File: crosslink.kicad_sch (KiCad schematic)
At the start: 2 parts, among them U9 CrossLink_LIF-MD6000-6JMG80I

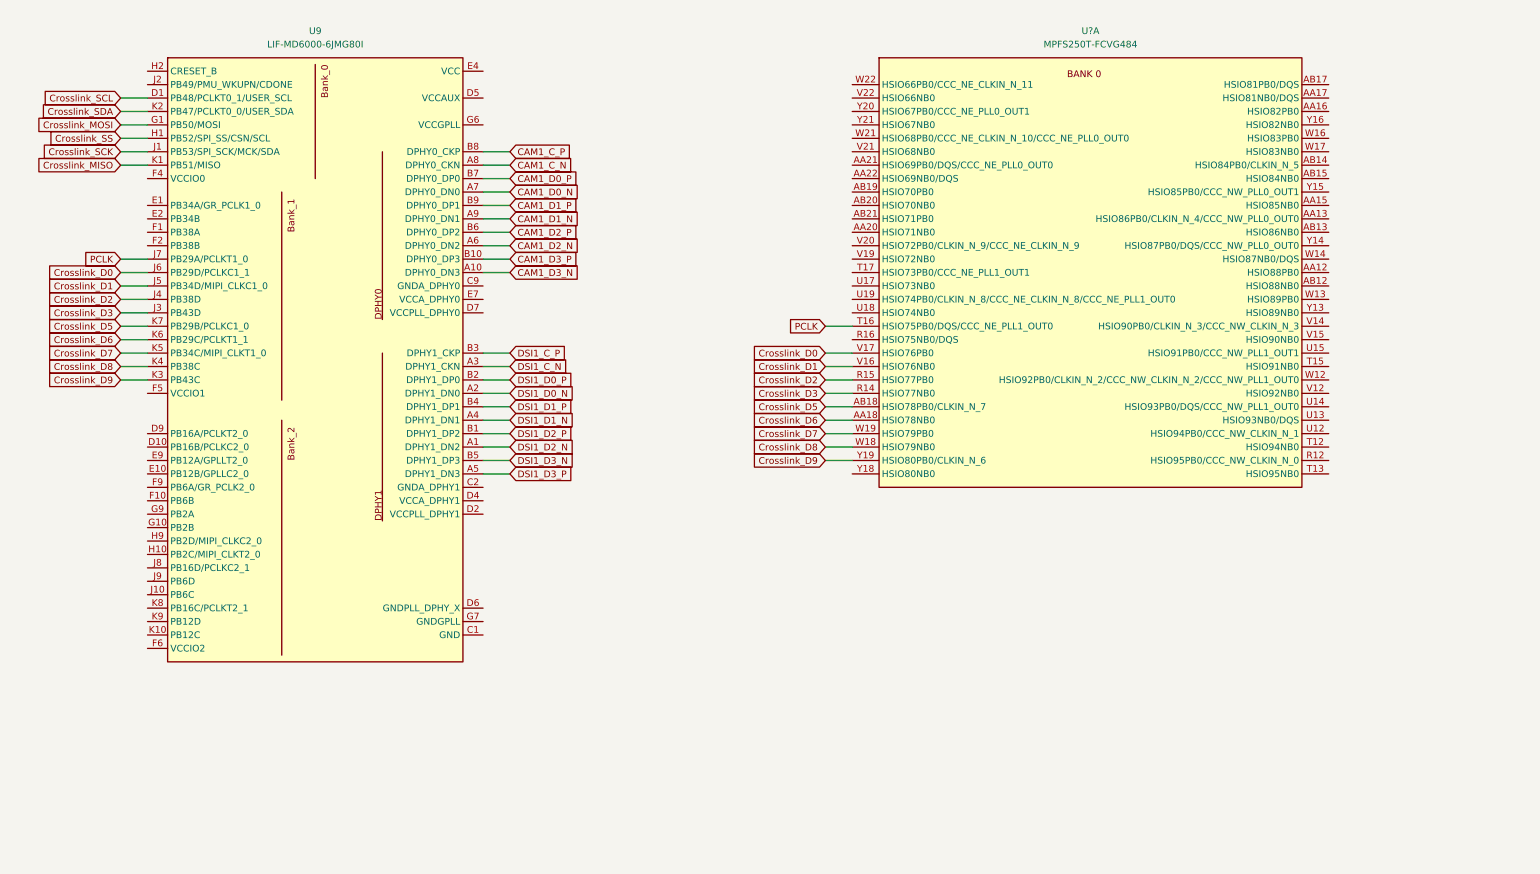
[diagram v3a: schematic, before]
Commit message: [#53847] Improve connection between Crosslink and PF
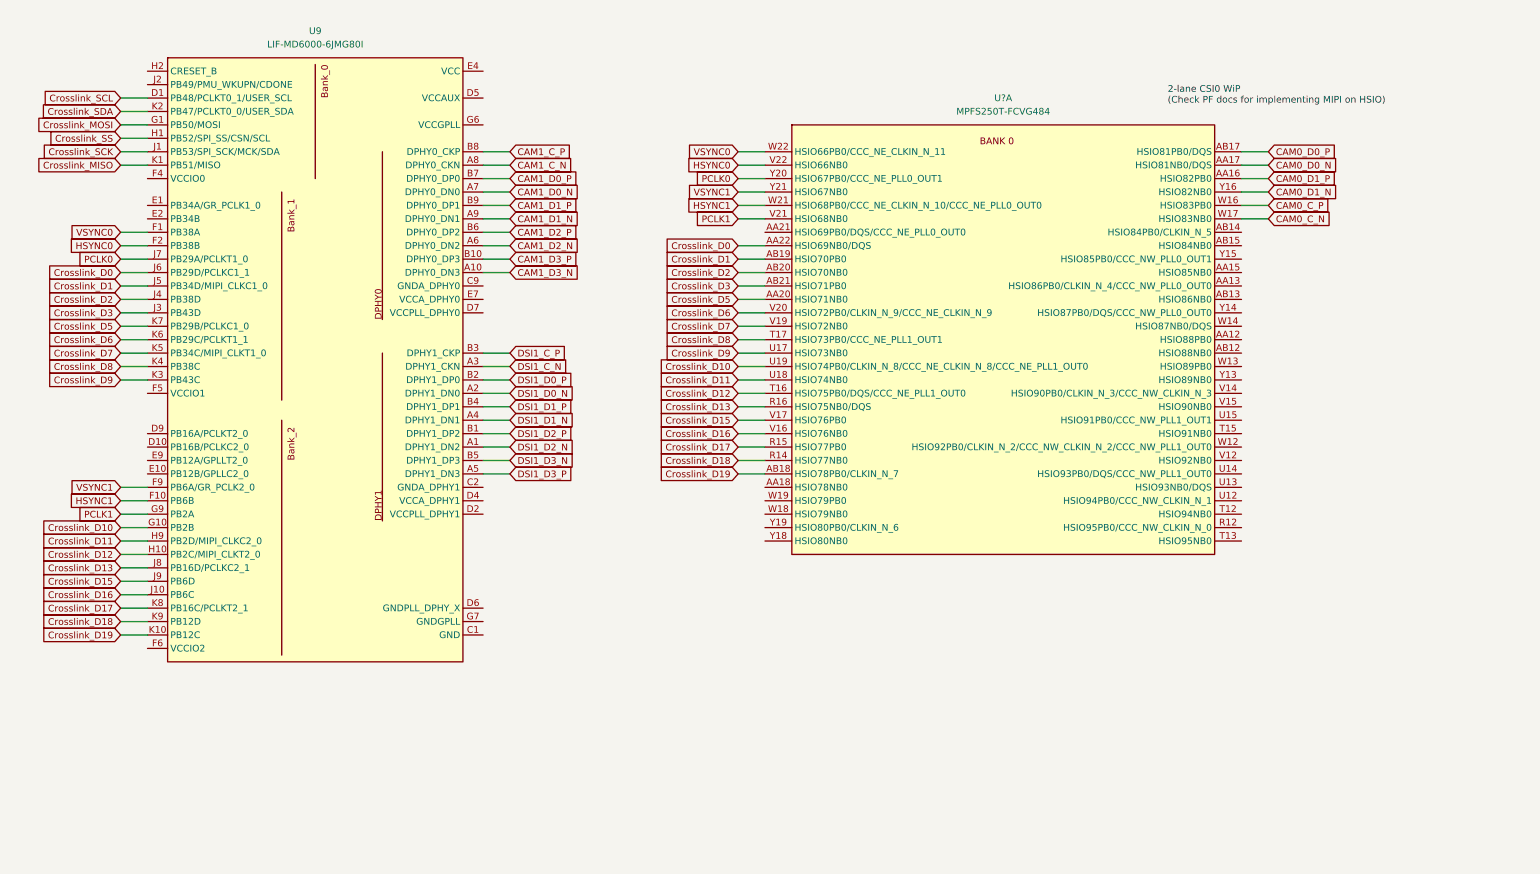
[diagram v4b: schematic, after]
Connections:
- net Crosslink_D0: now also U?.AA22 (HSIO69NB0/DQS); no longer U?.V17 (HSIO76PB0)
- net Crosslink_D1: now also U?.AB19 (HSIO70PB0); no longer U?.V16 (HSIO76NB0)
- net Crosslink_D2: now also U?.AB20 (HSIO70NB0); no longer U?.R15 (HSIO77PB0)
- net Crosslink_D3: now also U?.AB21 (HSIO71PB0); no longer U?.R14 (HSIO77NB0)
- net Crosslink_D5: now also U?.AA20 (HSIO71NB0); no longer U?.AB18 (HSIO78PB0/CLKIN_N_7)
- net Crosslink_D6: now also U?.V20 (HSIO72PB0/CLKIN_N_9/CCC_NE_CLKIN_N_9); no longer U?.AA18 (HSIO78NB0)
- net Crosslink_D7: now also U?.V19 (HSIO72NB0); no longer U?.W19 (HSIO79PB0)
- net Crosslink_D8: now also U?.T17 (HSIO73PB0/CCC_NE_PLL1_OUT1); no longer U?.W18 (HSIO79NB0)
- net Crosslink_D9: now also U?.U17 (HSIO73NB0); no longer U?.Y19 (HSIO80PB0/CLKIN_N_6)
- net CAM0_D1_P: now reaches U?.AA16 (HSIO82PB0)
- net CAM0_D0_N: now reaches U?.AA17 (HSIO81NB0/DQS)
- net CAM0_D0_P: now reaches U?.AB17 (HSIO81PB0/DQS)
- net Crosslink_D13: now reaches U?.R16 (HSIO75NB0/DQS)
- net Crosslink_D13: now also U9.J8 (PB16D/PCLKC2_1)
- net Crosslink_D11: now reaches U?.U18 (HSIO74NB0)
- net Crosslink_D11: now also U9.H9 (PB2D/MIPI_CLKC2_0)
- net Crosslink_D10: now reaches U?.U19 (HSIO74PB0/CLKIN_N_8/CCC_NE_CLKIN_N_8/CCC_NE_PLL1_OUT0)
- net Crosslink_D10: now also U9.G10 (PB2B)
- net PCLK1: now reaches U?.V21 (HSIO68NB0)
- net PCLK1: now also U9.G9 (PB2A)
- net HSYNC0: now reaches U?.V22 (HSIO66NB0)
- net HSYNC0: now also U9.F2 (PB38B)
- net CAM0_C_P: now reaches U?.W16 (HSIO83PB0)
- net CAM0_C_N: now reaches U?.W17 (HSIO83NB0)
- net HSYNC1: now reaches U?.W21 (HSIO68PB0/CCC_NE_CLKIN_N_10/CCC_NE_PLL0_OUT0)
- net HSYNC1: now also U9.F10 (PB6B)
- net VSYNC0: now reaches U?.W22 (HSIO66PB0/CCC_NE_CLKIN_N_11)
- net VSYNC0: now also U9.F1 (PB38A)
- net CAM0_D1_N: now reaches U?.Y16 (HSIO82NB0)
- net PCLK0: now reaches U?.Y20 (HSIO67PB0/CCC_NE_PLL0_OUT1)
- net PCLK0: now also U9.J7 (PB29A/PCLKT1_0)
- net VSYNC1: now reaches U?.Y21 (HSIO67NB0)
- net VSYNC1: now also U9.F9 (PB6A/GR_PCLK2_0)
- net Crosslink_D12: now reaches U9.H10 (PB2C/MIPI_CLKT2_0)
- net Crosslink_D12: now also U?.T16 (HSIO75PB0/DQS/CCC_NE_PLL1_OUT0)
- net Crosslink_D16: now reaches U9.J10 (PB6C)
- net Crosslink_D16: now also U?.V16 (HSIO76NB0)
- net Crosslink_D15: now reaches U9.J9 (PB6D)
- net Crosslink_D15: now also U?.V17 (HSIO76PB0)
- net Crosslink_D19: now reaches U9.K10 (PB12C)
- net Crosslink_D19: now also U?.AB18 (HSIO78PB0/CLKIN_N_7)
- net Crosslink_D17: now reaches U9.K8 (PB16C/PCLKT2_1)
- net Crosslink_D17: now also U?.R15 (HSIO77PB0)
- net Crosslink_D18: now reaches U9.K9 (PB12D)
- net Crosslink_D18: now also U?.R14 (HSIO77NB0)
- removed net PCLK: U9.J7 (PB29A/PCLKT1_0), U?.T16 (HSIO75PB0/DQS/CCC_NE_PLL1_OUT0)
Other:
- note added: "2-lane CSI0 WiP (Check PF docs for implementing MIPI on HSIO)"
- moved on the sheet: U?A

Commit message: [#53847] Add MIPI25 implementation of PF SoC
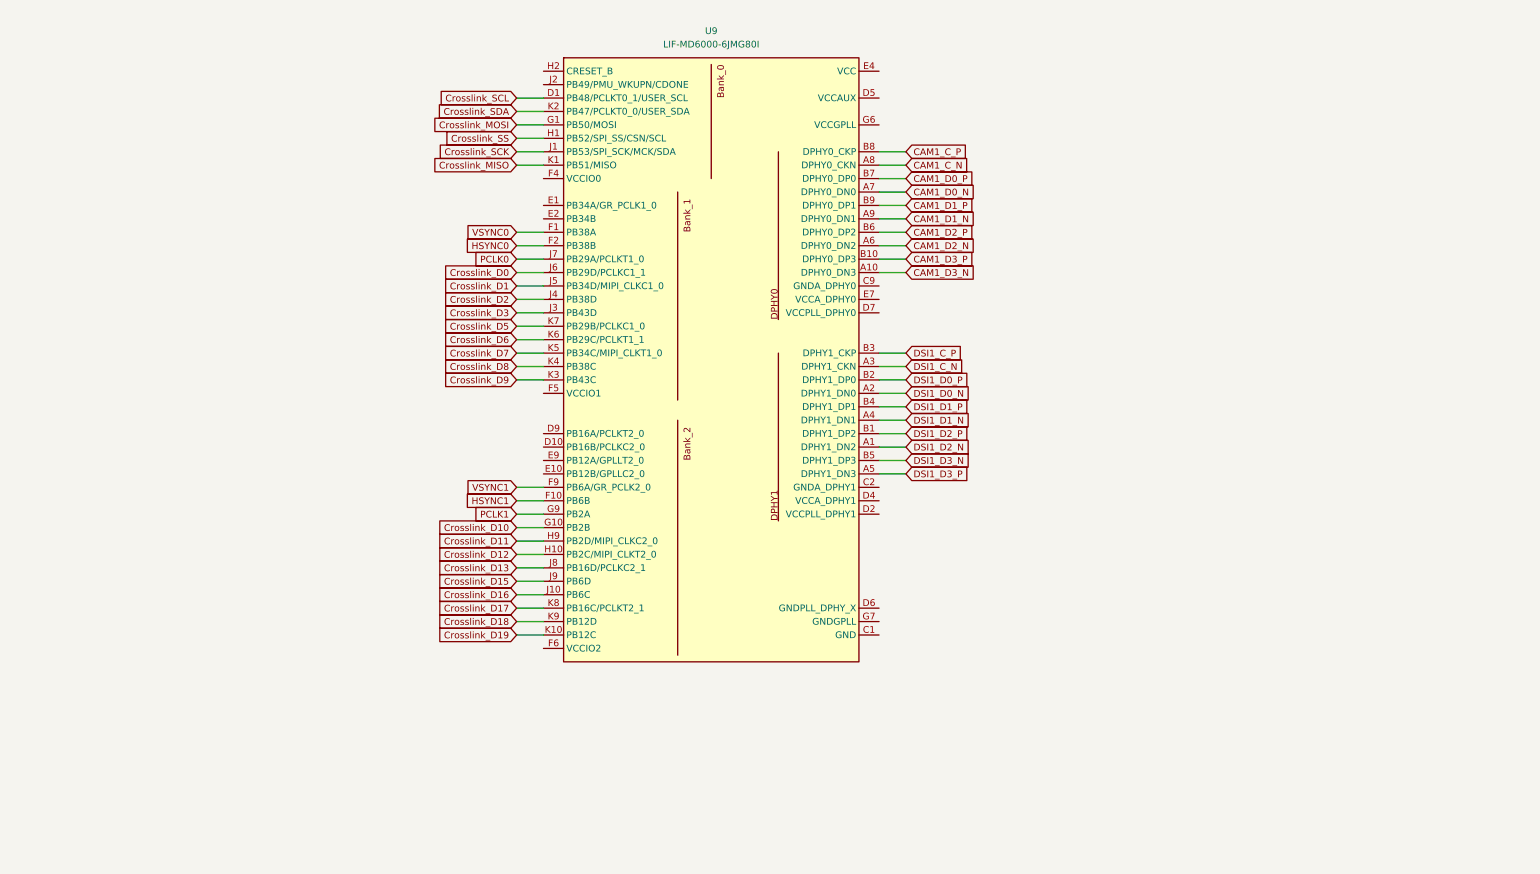
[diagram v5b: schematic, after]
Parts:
- removed U?: MPFS250T-FCVG484, antmicro-footprints:BGA-484_19x19mm_Layout22x22_P0.8mm_FCVG484, symbol antmicroMicrocontrollers:MPFS250T-FCVG484
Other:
- note removed: "2-lane CSI0 WiP (Check PF docs for implementing MIPI on HSIO)"
- moved on the sheet: U9

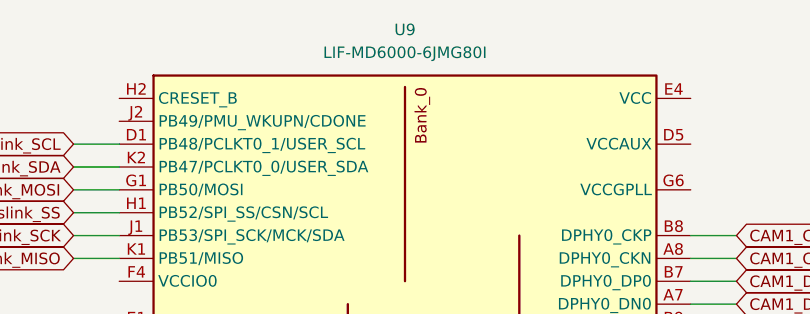
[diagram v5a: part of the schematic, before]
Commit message: [#52577] Clear annotations
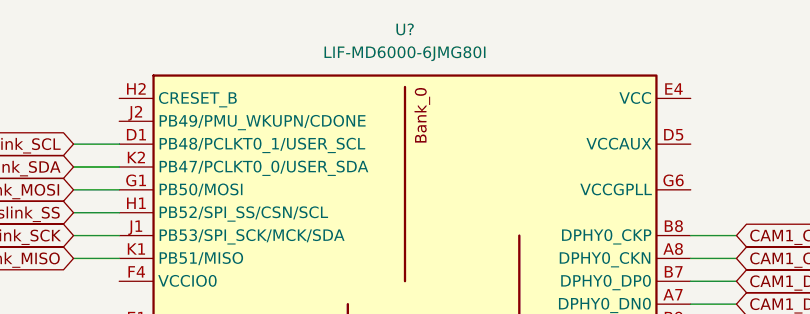
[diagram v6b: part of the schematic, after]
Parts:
- renumbered U9 to U?
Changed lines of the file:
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@@
   (symbol (lib_id "antmicroBGAchips:CrossLink_LIF-MD6000-6JMG80I") (at 118.11 45.72 0) (unit 1)
     (in_bom yes) (on_board yes) (fields_autoplaced)
-    (property "Reference" "U9" (id 0) (at 149.86 38.1 0)
+    (property "Reference" "U?" (id 0) (at 149.86 38.1 0)
       (effects (font (size 1.27 1.27) (thickness 0.15)))
     )

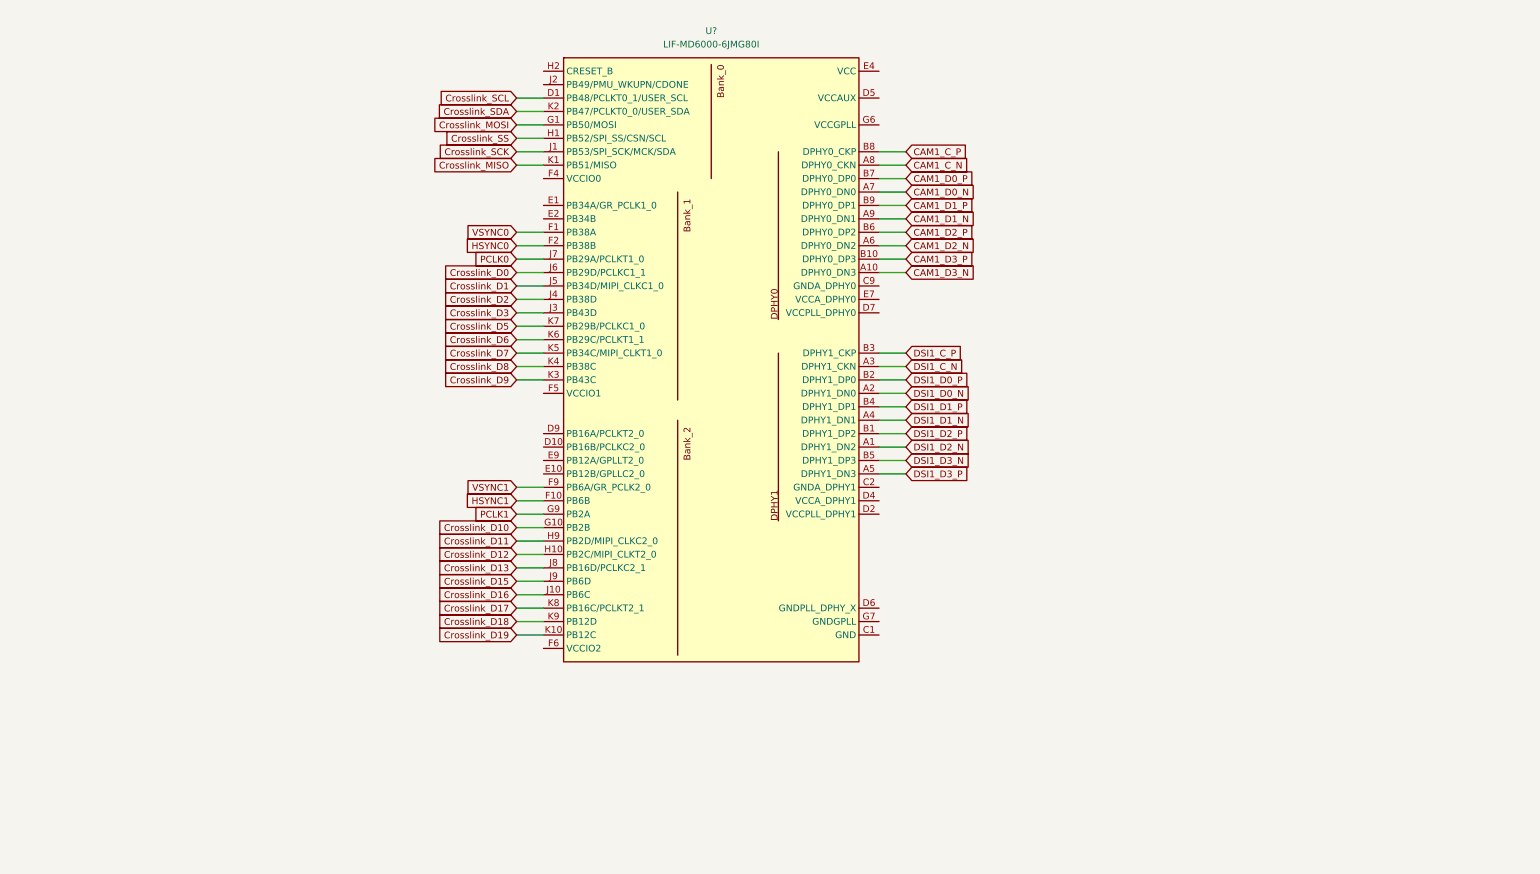
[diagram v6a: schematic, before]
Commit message: [#54084] Sheets cleanup
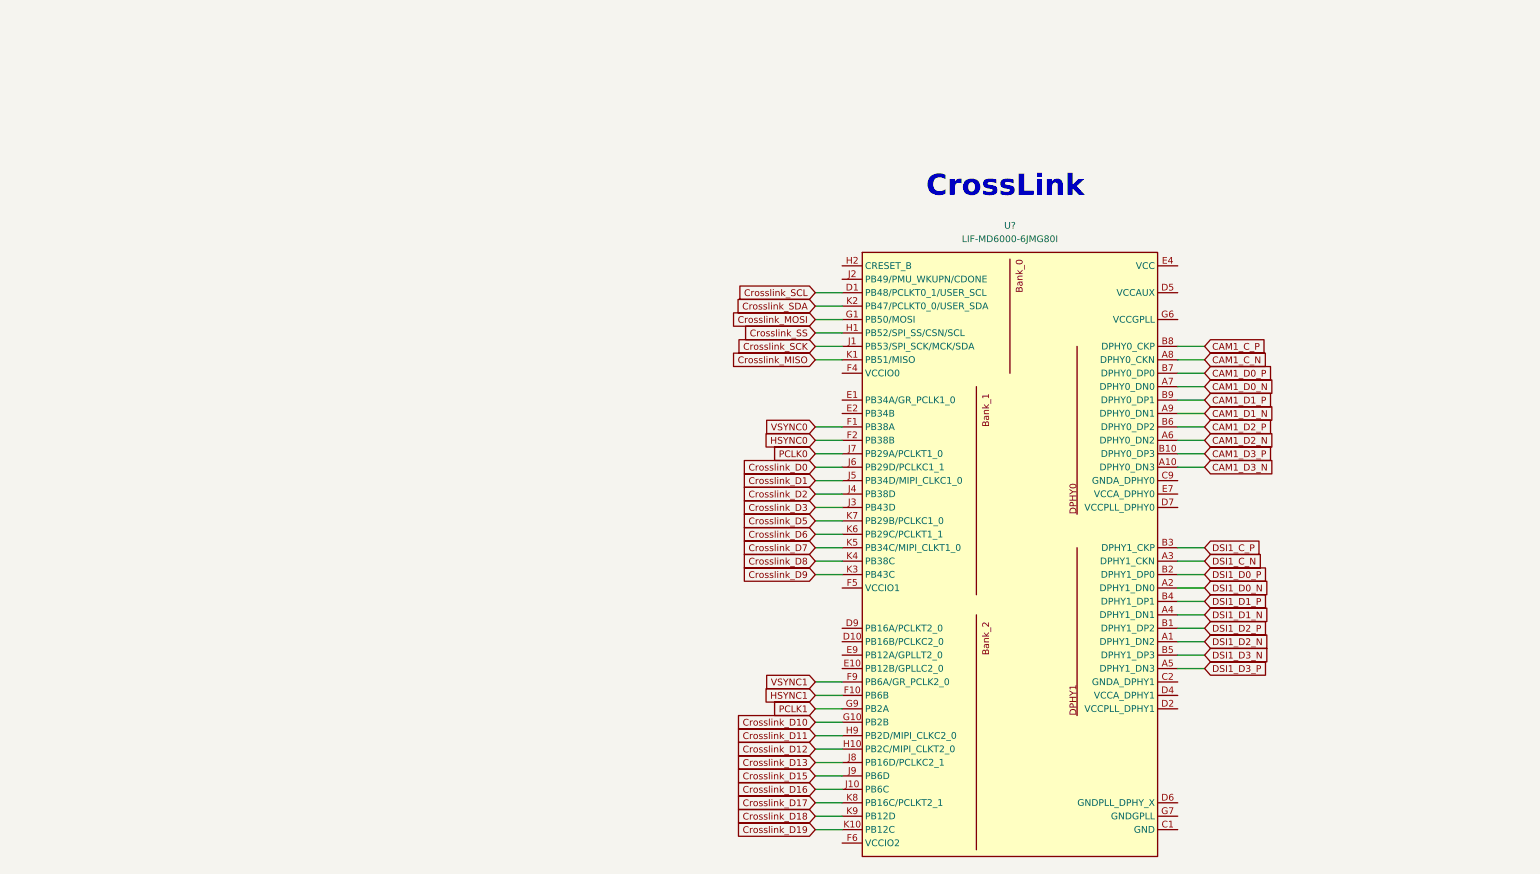
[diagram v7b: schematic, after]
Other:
- note added: "CrossLink"
- company: (none) -> Antmicro Ltd
- title: (none) -> PolarFire SoM
- moved on the sheet: U?

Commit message: [#54016] Connect power to CrossLink
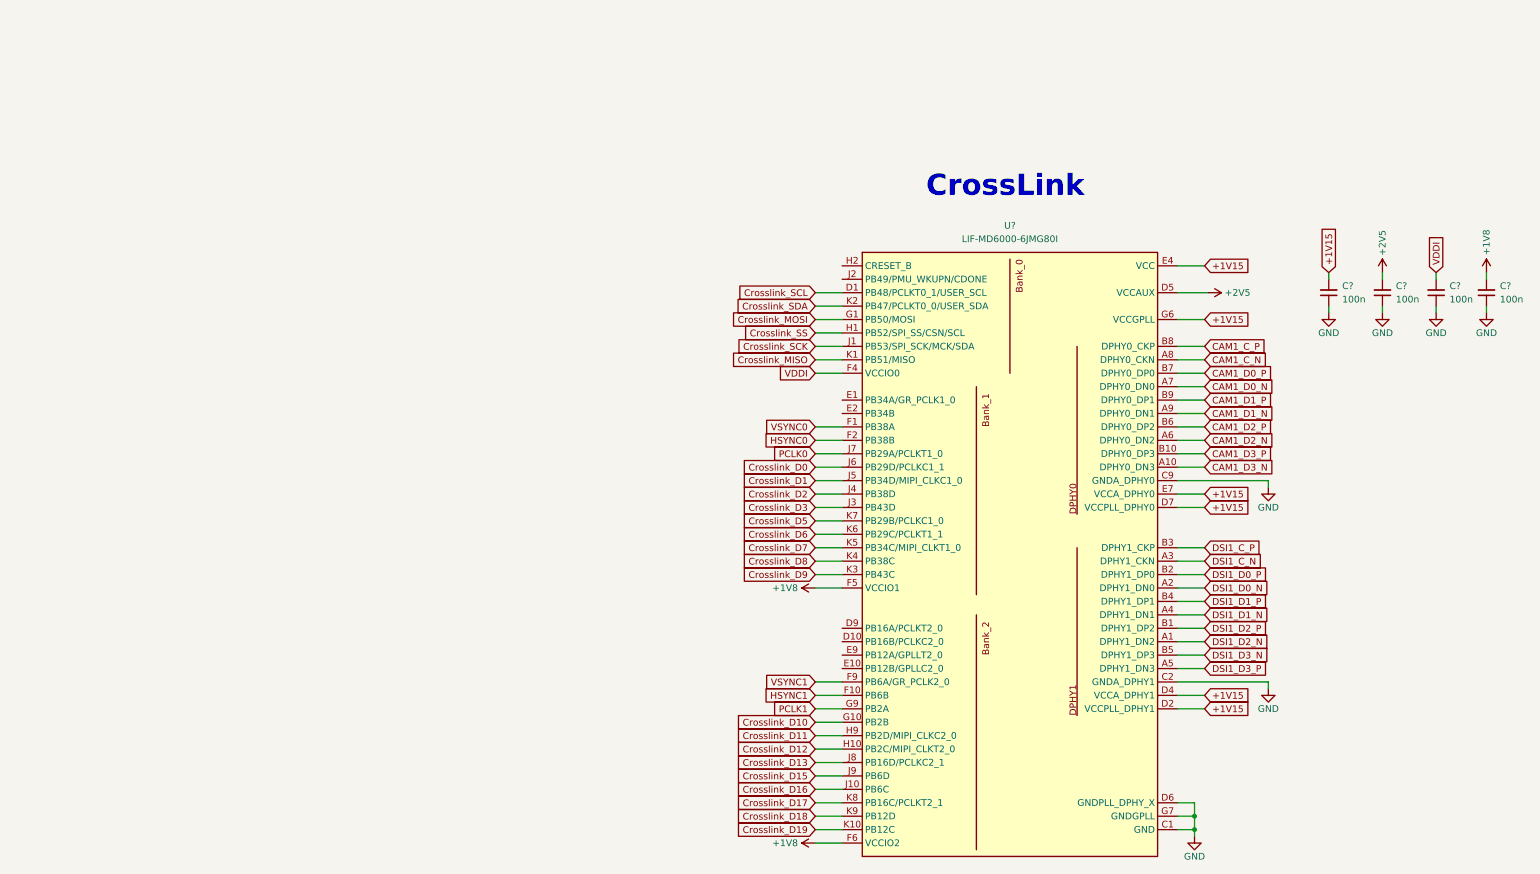
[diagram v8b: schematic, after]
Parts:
- added C? (x4): C_100n_0402, antmicro-footprints:C_0402_1005Metric, symbol antmicroCapacitors0402:C_100n_0402
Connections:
- net GND: now reaches U?.C1 (GND), U?.C10 (GND), U?.E5 (GND), U?.G2 (GND), U?.G5 (GND)
- net GND: now also U?.C2 (GNDA_DPHY1), U?.C9 (GNDA_DPHY0), U?.D6 (GNDPLL_DPHY_X), U?.G7 (GNDGPLL), C?.1, C?.1, C?.1, C?.1
- net +1V15: now reaches U?.D2 (VCCPLL_DPHY1)
- net +1V15: now also U?.D4 (VCCA_DPHY1), U?.D7 (VCCPLL_DPHY0), U?.E4 (VCC), U?.E6 (VCC), U?.E7 (VCCA_DPHY0), U?.G6 (VCCGPLL), C?.2
- net +2V5: now reaches U?.D5 (VCCAUX)
- net +2V5: now also C?.2
- net VDDI: now reaches U?.F4 (VCCIO0)
- net VDDI: now also C?.2
- net +1V8: now reaches U?.F5 (VCCIO1), U?.G4 (VCCIO1)
- net +1V8: now also U?.F6 (VCCIO2), U?.F7 (VCCIO2), C?.2
